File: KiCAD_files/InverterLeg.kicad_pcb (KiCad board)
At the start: 4 copper layers, 29 x 73 mm, 100 parts, among them J801 Conn_Coaxial_Small, J802 Conn_Coaxial_Small, J804 Conn_01x03_Socket, J811 Screw_Terminal_01x01, J814 Screw_Terminal_01x01, J817 Screw_Terminal_01x01, J825 HC-PBB08-2-08-M-H4.0-G1-R-P-04, J827 HC-PBB08-2-08-M-H4.0-G1-R-P-04, J831 HC-PBB08-2-08-M-H4.0-G1-R-P-04, T801 TE1212-2W6ENT, T802 TE1212-2W6ENT, U603 UCC21520, U704 VPS8701B, U707 VPS8701B, U801 LT1761-SD, U802 LT1761-SD, U811 TMP117xxDRV, U815 TMP117xxDRV

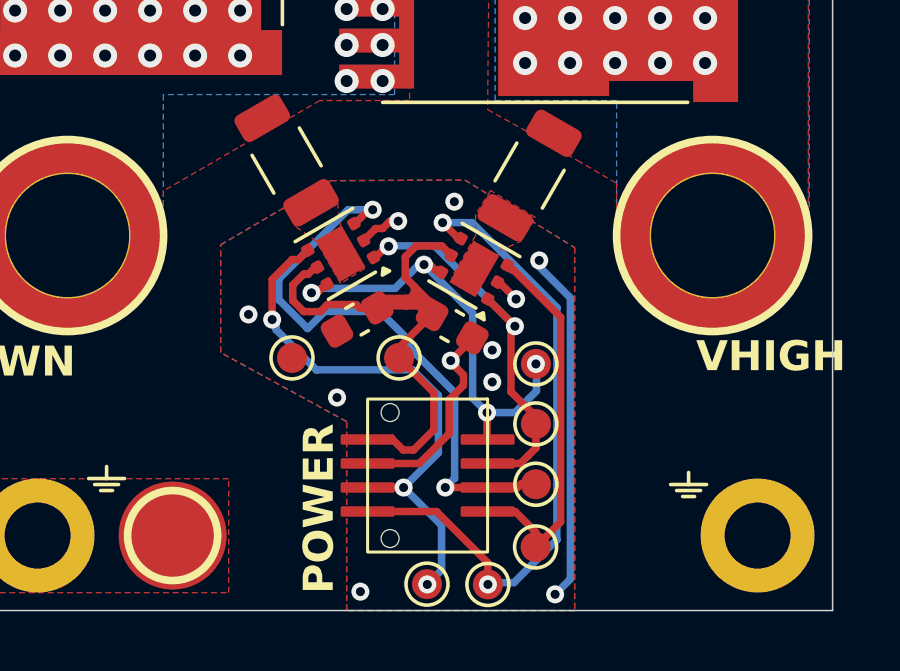
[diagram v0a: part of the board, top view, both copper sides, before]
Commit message: Added an EEPROM footprint. Mooved slightly thermal sensor connector.
Signed-off-by: Jean Alinei <jean.alinei@owntech.org>
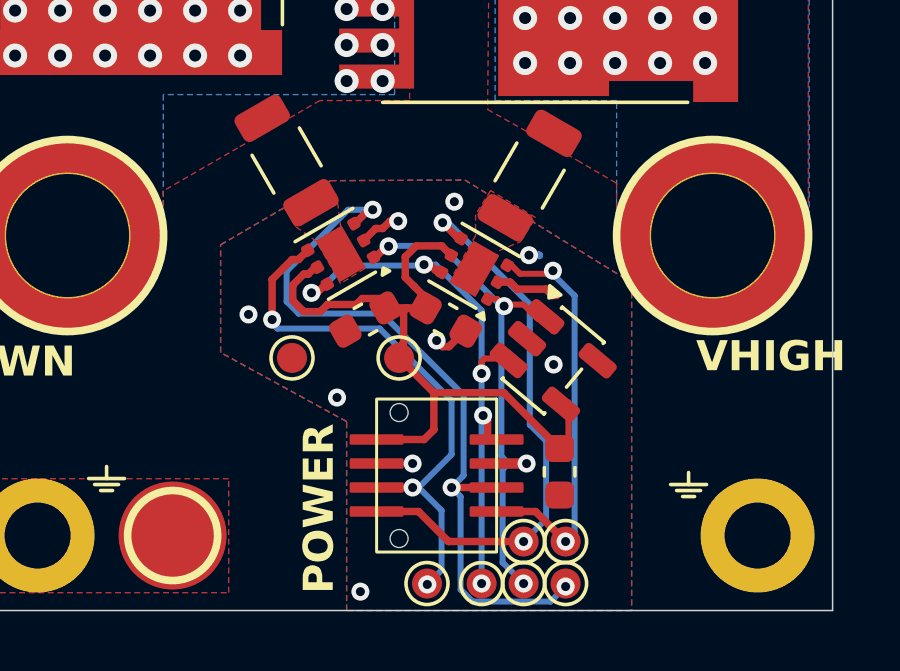
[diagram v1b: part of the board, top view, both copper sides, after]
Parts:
- added C755: 100nF, Capacitor_SMD:C_0603_1608Metric, F.Cu at (151.9, 132.4)
- added U803: 24CS02, Package_TO_SOT_SMD:SOT-23-5, F.Cu at (151.7, 128.7)
- moved TP815 7.54 mm to (149.3, 136.1)
- moved TP816 5.34 mm to (150.7, 136.1)
- moved TP817 3.45 mm to (152.1, 136.1)
- moved TP822 1.86 mm to (150.7, 134.7)
- moved TP818 1.02 mm to (152.1, 134.7)
- moved C751 0.31 mm to (148.1, 127.3)
- moved J827 0.30 mm to (147.8, 132.5)
- moved C754 0.28 mm to (145.4, 127.3)
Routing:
- net PGND: track 21.5 -> 5.42 mm, vias 11 -> 9
- net /SCL_{PWR}: track 13.5 -> 19.0 mm, vias 2 -> 4
- net /ALERT_LS: track 19.7 -> 24.8 mm, vias 2 -> 3
- net +5V_PGND: track 18.9 -> 23.7 mm
- net /SDA_{PWR}: track 15.0 -> 19.4 mm, vias 4 -> 5
- net /ADDR_HS: track 21.8 -> 18.8 mm
- net /ALERT_HS: track 12.9 -> 14.1 mm, vias 0 -> 2
- net /ADDR_LS: track 18.4 -> 18.9 mm

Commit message: Changed signal connectors to male parts. Updated the 3D models.
Signed-off-by: Jean Alinei <jean.alinei@owntech.org>
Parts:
- C607, C608: value 100nF -> 1nF
- D601, D602, D703, D704, D709, D710: value PMEG4010 -> PMEG4010ESBYL
- J801, J802: value Conn_Coaxial_Small -> AIPEX-4
- J803, J806: value ~ -> 2LC000-739
- J811, J814, J817: value Screw_Terminal_01x01 -> SMTSO3050CTJ
- J825, J827, J831: value HC-PBB08-2-08-M-H4.0-G1-R-P-04 -> HC-PBB08-2-08-M-H1.0-G1-R-P-04; footprint Footprints:HC-PBB02-2-08-M -> Footprints:HC-PBB02-2-08-Male
- Q801, Q802: value ~ -> AGM15T05LL
- T801, T802: value TE1212-2W6ENT -> TE1212-1W6ENT
- TJ801, TJ804: value ~ -> THJP1206AST1
- U603: value UCC21520 -> UCC21520DWR
- U801, U802: value LT1761-SD -> SY6345AAC
- U803: value 24CS02 -> 24C02S(XBLW)
- U811, U815: value TMP117xxDRV -> T117B

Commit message: Fixed ADJ resistors values.
Signed-off-by: Jean Alinei <jean.alinei@owntech.org>
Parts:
- R610, R612: value 178k -> 510k
- R611, R613: value 20k -> 27k
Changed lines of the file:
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@@
 			)
 		)
-		(property "Value" "20k"
+		(property "Value" "27k"
 			(at 0 1.17 90)
 			(layer "F.Fab")
@@
 			)
 		)
-		(property "Description" "20 kohm +/-1%, 62.5 mW thick-film resistor, 0402; UNI-ROYAL 0402WGF2002TCE"
+		(property "Description" "27 kohm +/-1%, 62.5 mW thick-film resistor, 0402; UNI-ROYAL 0402WGF2002TCE"
 			(at 0 0 90)
 			(layer "F.Fab")
@@
 			)
 		)
-		(property "LCSC" "C25765"
+		(property "LCSC" "C25771"
 			(at 0 0 90)
 			(unlocked yes)
@@
 			)
 		)
-		(property "Value" "178k"
+		(property "Value" "510k"
 			(at 0 1.17 90)
 			(layer "F.Fab")
@@
 			)
 		)
-		(property "Description" "178 kohm +/-1%, 62.5 mW thick-film resistor, 0402; UNI-ROYAL 0402WGF1783TCE"
+		(property "Description" "510 kohm +/-1%, 62.5 mW thick-film resistor, 0402; UNI-ROYAL 0402WGF1783TCE"
 			(at 0 0 90)
 			(layer "F.Fab")
@@
 			)
 		)
-		(property "LCSC" "C26995"
+		(property "LCSC" "C11616"
 			(at 0 0 90)
 			(unlocked yes)
@@
 			)
 		)
-		(property "Value" "20k"
+		(property "Value" "27k"
 			(at 0 1.17 90)
 			(layer "F.Fab")
@@
 			)
 		)
-		(property "Description" "20 kohm +/-1%, 62.5 mW thick-film resistor, 0402; UNI-ROYAL 0402WGF2002TCE"
+		(property "Description" "27 kohm +/-1%, 62.5 mW thick-film resistor, 0402; UNI-ROYAL 0402WGF2002TCE"
 			(at 0 0 90)
 			(layer "F.Fab")
@@
 			)
 		)
-		(property "LCSC" "C25765"
+		(property "LCSC" "C25771"
 			(at 0 0 90)
 			(unlocked yes)
@@
 		(sheetname "/")
 		(sheetfile "InverterLeg.kicad_sch")
+		(units
+			(unit
+				(name "A")
+				(pins "1" "2" "3" "4" "8" "7" "6" "5")
+			)
+		)
 		(attr board_only)
 		(duplicate_pad_numbers_are_jumpers no)
@@
 		(sheetname "/")
 		(sheetfile "InverterLeg.kicad_sch")
+		(units
+			(unit
+				(name "A")
+				(pins "1" "2" "3" "4" "8" "7" "6" "5")
+			)
+		)
 		(attr board_only)
 		(duplicate_pad_numbers_are_jumpers no)
@@
 			)
 		)
-		(property "Value" "178k"
+		(property "Value" "510k"
 			(at 0 1.17 90)
 			(layer "F.Fab")
@@
 			)
 		)
-		(property "Description" "178 kohm +/-1%, 62.5 mW thick-film resistor, 0402; UNI-ROYAL 0402WGF1783TCE"
+		(property "Description" "510 kohm +/-1%, 62.5 mW thick-film resistor, 0402; UNI-ROYAL 0402WGF1783TCE"
 			(at 0 0 90)
 			(layer "F.Fab")
@@
 			)
 		)
-		(property "LCSC" "C26995"
+		(property "LCSC" "C11616"
 			(at 0 0 90)
 			(unlocked yes)
@@
 		(sheetname "/")
 		(sheetfile "InverterLeg.kicad_sch")
+		(units
+			(unit
+				(name "A")
+				(pins "1" "2" "3" "4" "8" "7" "6" "5")
+			)
+		)
 		(attr board_only)
 		(duplicate_pad_numbers_are_jumpers no)

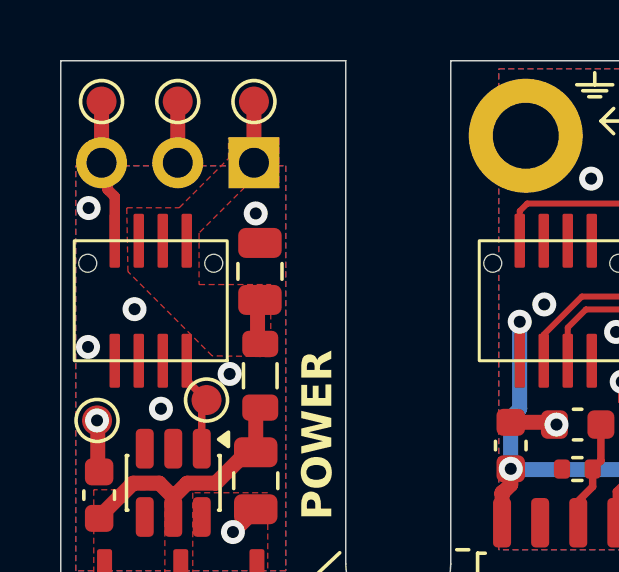
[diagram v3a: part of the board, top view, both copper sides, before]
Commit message: Added FAN_ON pins.
Signed-off-by: Jean Alinei <jean.alinei@owntech.org>
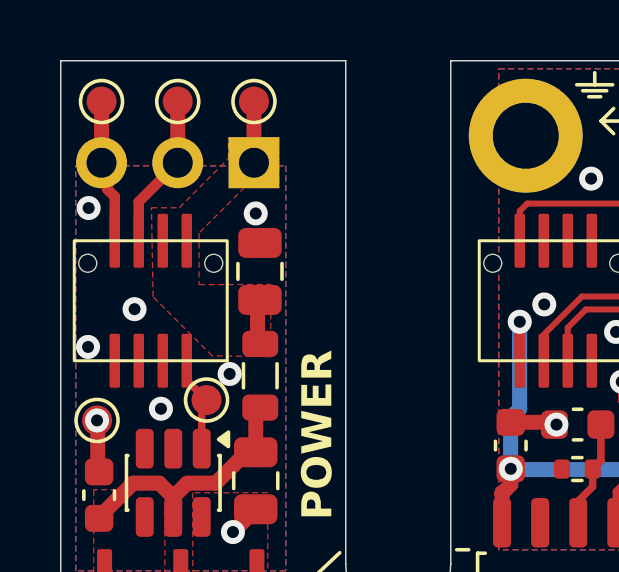
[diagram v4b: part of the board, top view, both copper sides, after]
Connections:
- J804 pad 2: PGND2 -> /FAN_{ON}
- J825 pad 3: +12V_PGND -> /FAN_{ON}
- TP808 pad 1: PGND2 -> /FAN_{ON}
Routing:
- net /FAN_{ON}: track 0.00 -> 5.18 mm
- net PGND2: track 4.86 -> 2.82 mm
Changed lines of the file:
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@@
 			)
 		)
-		(property "Datasheet" "${KIPRJMOD}\\datasheet\\cr-1858361.pdf"
+		(property "Datasheet" ""
 			(at 0 0 90)
 			(layer "F.Fab")
@@
 			)
 		)
-		(property "Datasheet" "${KIPRJMOD}\\datasheet\\cr-1858361.pdf"
+		(property "Datasheet" ""
 			(at 0 0 90)
 			(layer "F.Fab")
@@
 			(layers "F.Cu" "F.Mask" "F.Paste")
 			(roundrect_rratio 0.15)
-			(net "+12V_PGND")
+			(net "/FAN_{ON}")
 			(pinfunction "Pin_3_3")
 			(pintype "passive")
@@
 			(size 1 1)
 			(layers "F.Cu" "F.Mask")
-			(net "PGND2")
+			(net "/FAN_{ON}")
 			(pinfunction "1_1")
 			(pintype "passive")
@@
 			)
 		)
-		(property "Datasheet" "${KIPRJMOD}\\datasheet\\cr-1858361.pdf"
+		(property "Datasheet" ""
 			(at 0 0 90)
 			(layer "F.Fab")
@@
 			(layers "*.Cu" "*.Mask")
 			(remove_unused_layers no)
-			(net "PGND2")
+			(net "/FAN_{ON}")
 			(pinfunction "Pin_2_2")
 			(pintype "passive")
@@
 	)
 	(segment
-		(start 135.9 65.36)
-		(end 135.9 67.4)
-		(width 0.5)
-		(layer "F.Cu")
-		(net "PGND2")
-	)
-	(segment
 		(start 137.74 79.71)
 		(end 138.5 78.95)
@@
 		(net "Net-(U603-INA)")
 	)
+	(segment
+		(start 135.9 67.4)
+		(end 134.6 68.7)
+		(width 0.35)
+		(layer "F.Cu")
+		(net "/FAN_{ON}")
+	)
+	(segment
+		(start 135.9 65.36)
+		(end 135.9 67.4)
+		(width 0.5)
+		(layer "F.Cu")
+		(net "/FAN_{ON}")
+	)
+	(segment
+		(start 134.6 68.7)
+		(end 134.6 70)
+		(width 0.35)
+		(layer "F.Cu")
+		(net "/FAN_{ON}")
+	)
 	(zone
 		(net "Net-(D710-A)")
@@
 		(polygon
 			(pts
-				(xy 134.2 68.9) (xy 135.95 68.9) (xy 137.59 67.26) (xy 137.59 66.58) (xy 139.27 66.58) (xy 139.27 68.22)
+				(xy 135.023078 68.9) (xy 135.95 68.9) (xy 137.59 67.26) (xy 137.59 66.58) (xy 139.27 66.58) (xy 139.27 68.22)
 				(xy 138.13 68.22) (xy 136.61 69.74) (xy 136.61 71.46) (xy 139 71.46) (xy 139 73.863219) (xy 137.046874 73.836874)
-				(xy 134.239538 71.029538)
+				(xy 135.078186 71.868186)
 			)
 		)

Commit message: modifed the silk for the connectors, and edited the footprint and symbol for gate connector probing
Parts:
- removed kibuzzard-6A8EFBEE: G***, kibuzzard-6A8EFBEE
- added kibuzzard-6AA2AEDD: G***, kibuzzard-6AA2AEDD, B.Cu at (135.9, 64.9)
- R610, R612: value 510k -> 158k
- R611, R613: value 27k -> 10k
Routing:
- net /K_{GNDLS}: track 12.1 -> 12.8 mm
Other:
- board text added: "FANON"
